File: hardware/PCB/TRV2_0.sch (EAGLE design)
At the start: 48 parts, among them IC1 TMP112, IC2 SHT21, IC4 CNY70, IC5 ATMEGA8-AU, Q1 FC-12M

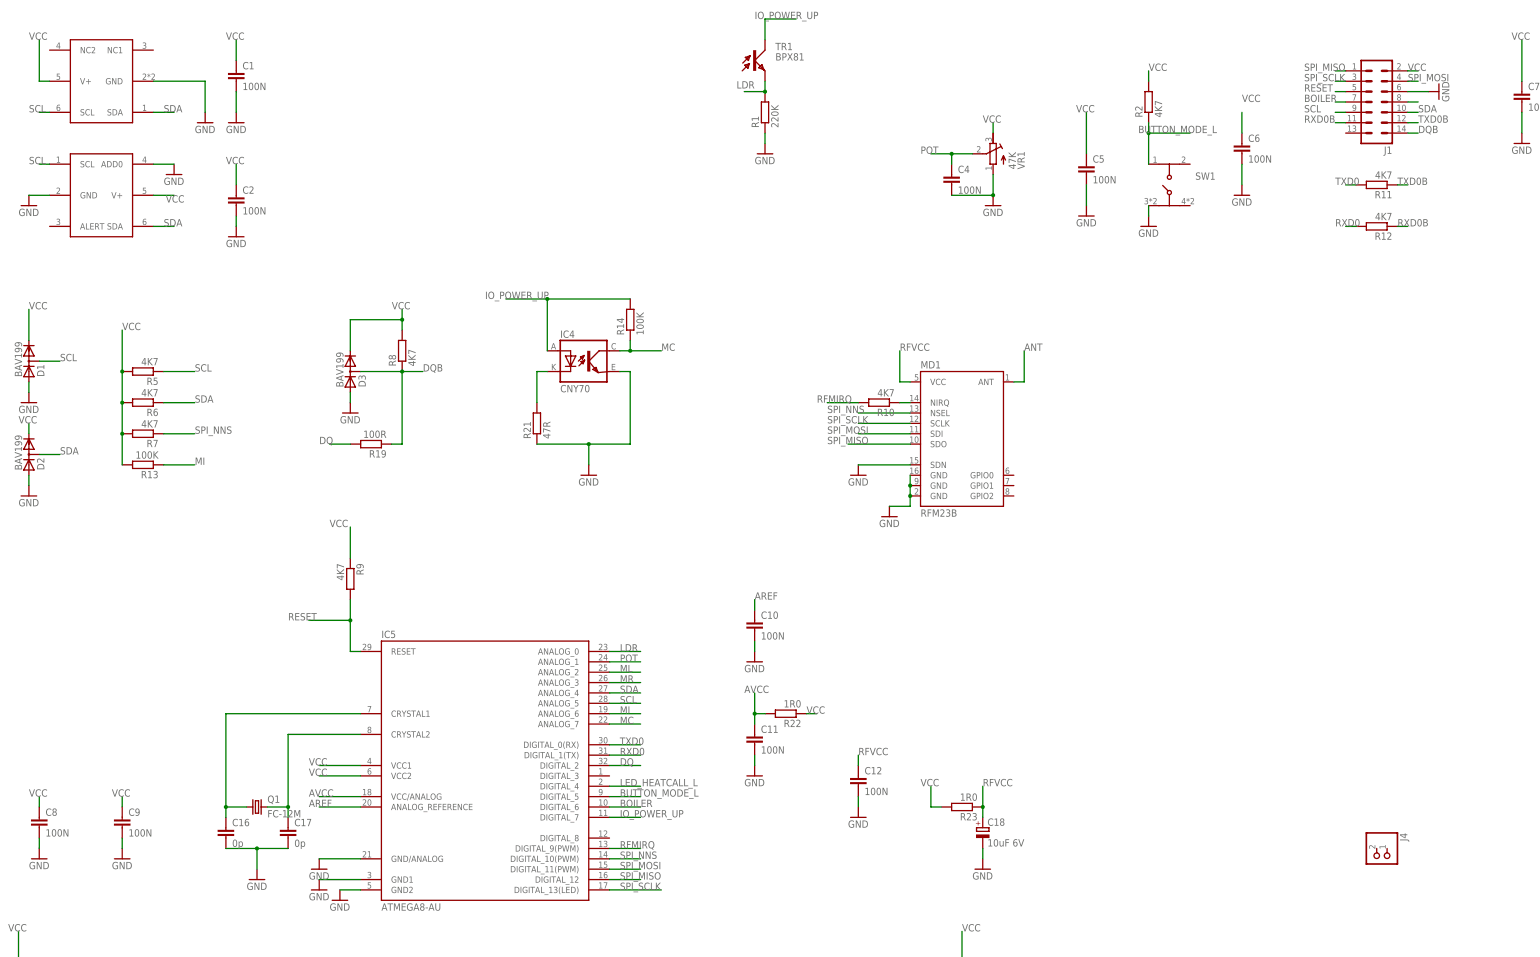
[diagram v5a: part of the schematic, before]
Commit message: removed RFM
8 pin header is just placeholder for now
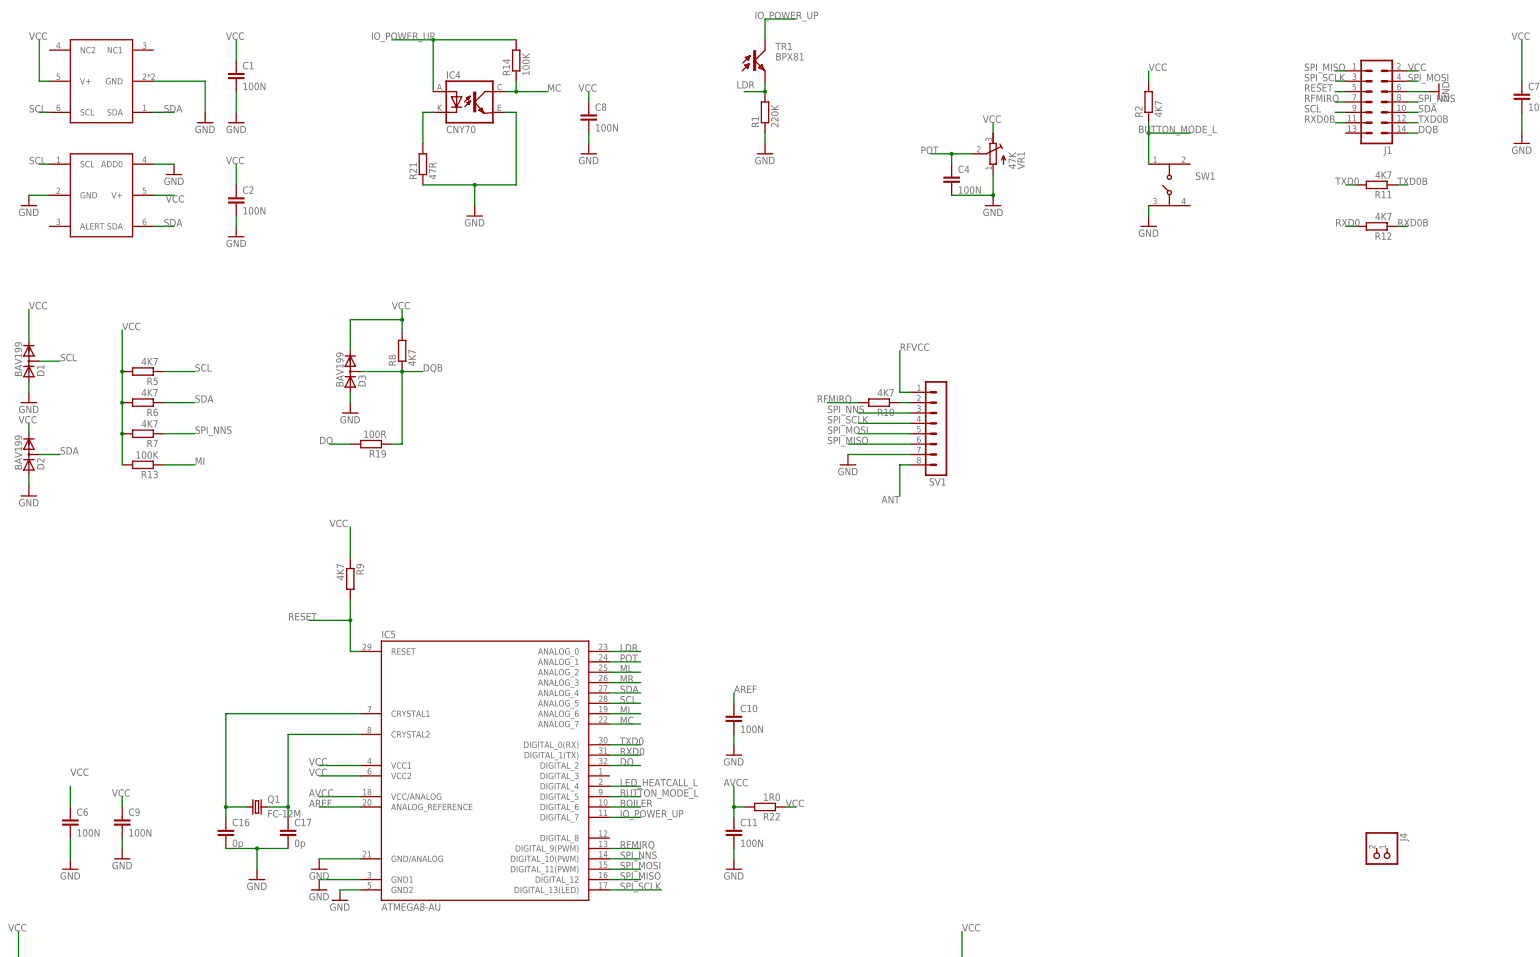
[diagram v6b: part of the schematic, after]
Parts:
- removed C12, C5: 100N, rcl:C-EUC0603
- removed C18: 10uF 6V, resistor:CPOL-EUSMCB
- removed MD1: RFM23B, SparkFun-RF:RFM23B
- removed R23: 1R0, resistor:R-EU_R0603
- added SV1: (no value), con-lstb:MA08-1
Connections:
- removed net N$2: J1.8
- net ANT: now also SV1.8; no longer MD1.ANT
- net BOILER: no longer J1.7
- net GND: now also SV1.7; no longer C12.2, C18.-, C5.2, MD1.GND@1, MD1.GND@2, MD1.GND@3, MD1.SDN
- net N$3: now also SV1.2; no longer MD1.NIRQ
- net RFMIRQ: now also J1.7
- net RFVCC: now also SV1.1; no longer C12.1, C18.+, MD1.VCC, R23.1
- net SPI_MISO: now also SV1.6; no longer MD1.SDO
- net SPI_MOSI: now also SV1.5; no longer MD1.SDI
- net SPI_NNS: now also J1.8, SV1.3; no longer MD1.NSEL
- net SPI_SCLK: now also SV1.4; no longer MD1.SCLK
- net VCC: no longer C5.1, R23.2
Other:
- moved on the sheet: C10, C11, C6, C8, IC4, R14, R21, R22

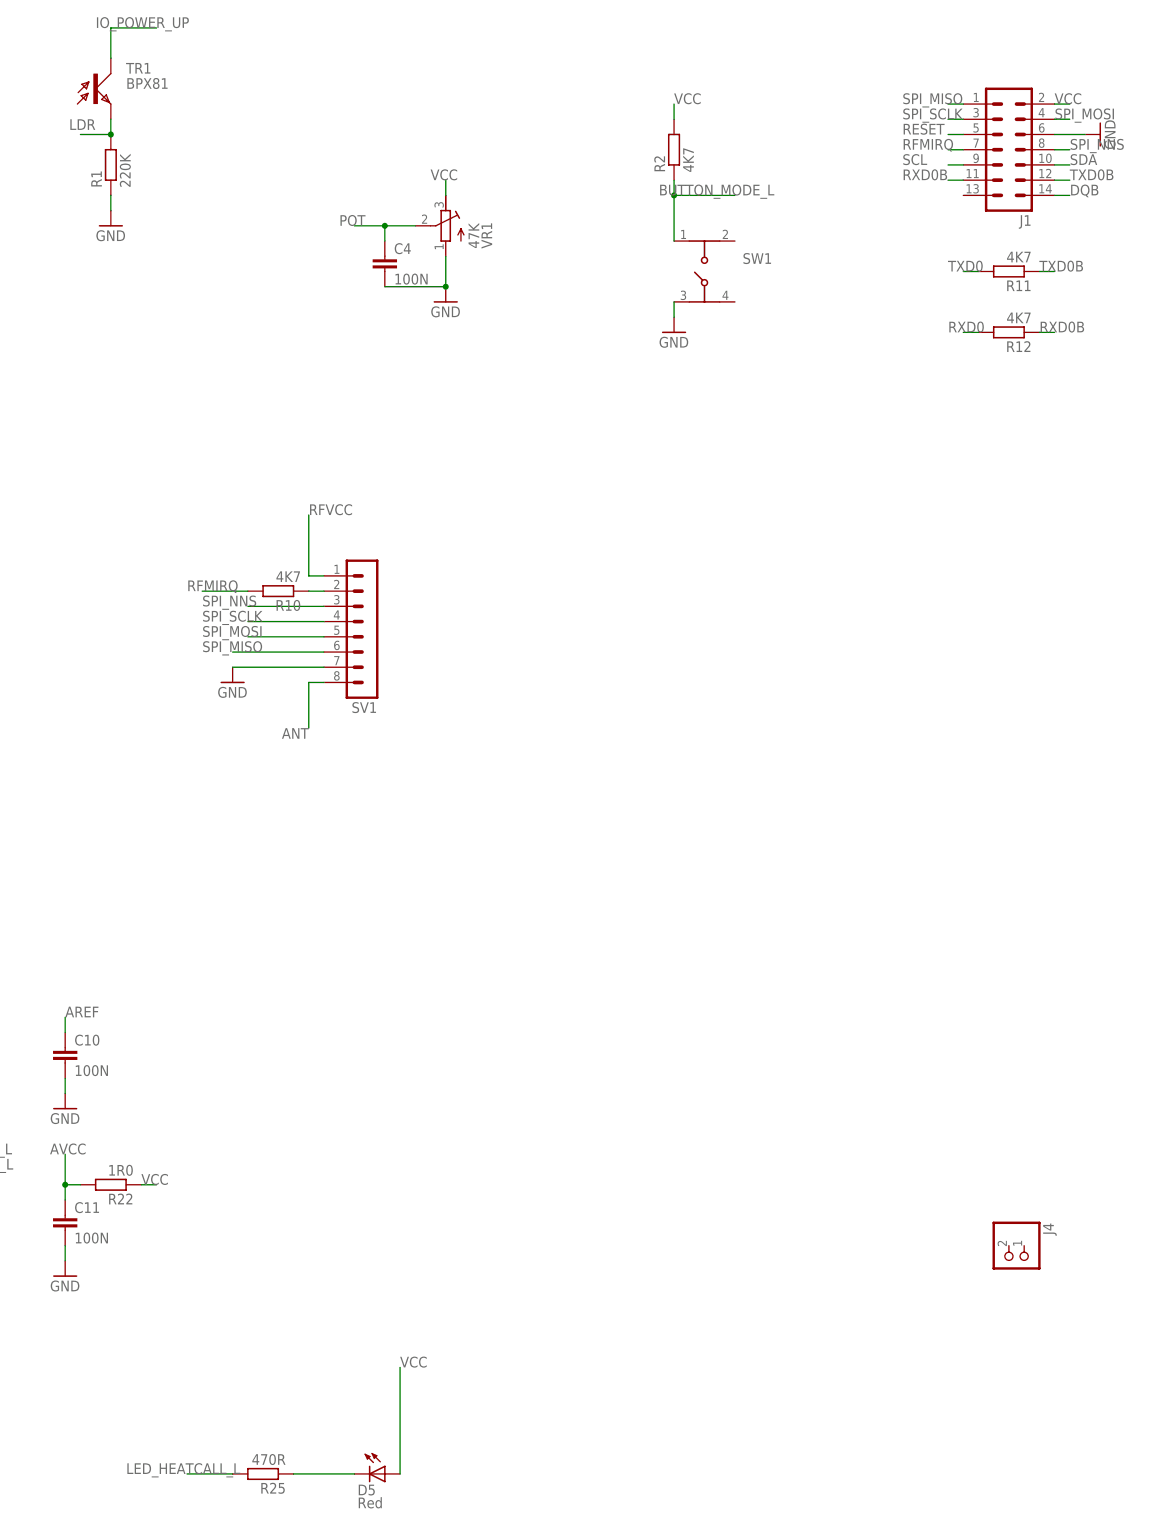
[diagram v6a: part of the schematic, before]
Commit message: SMD LED and photo added
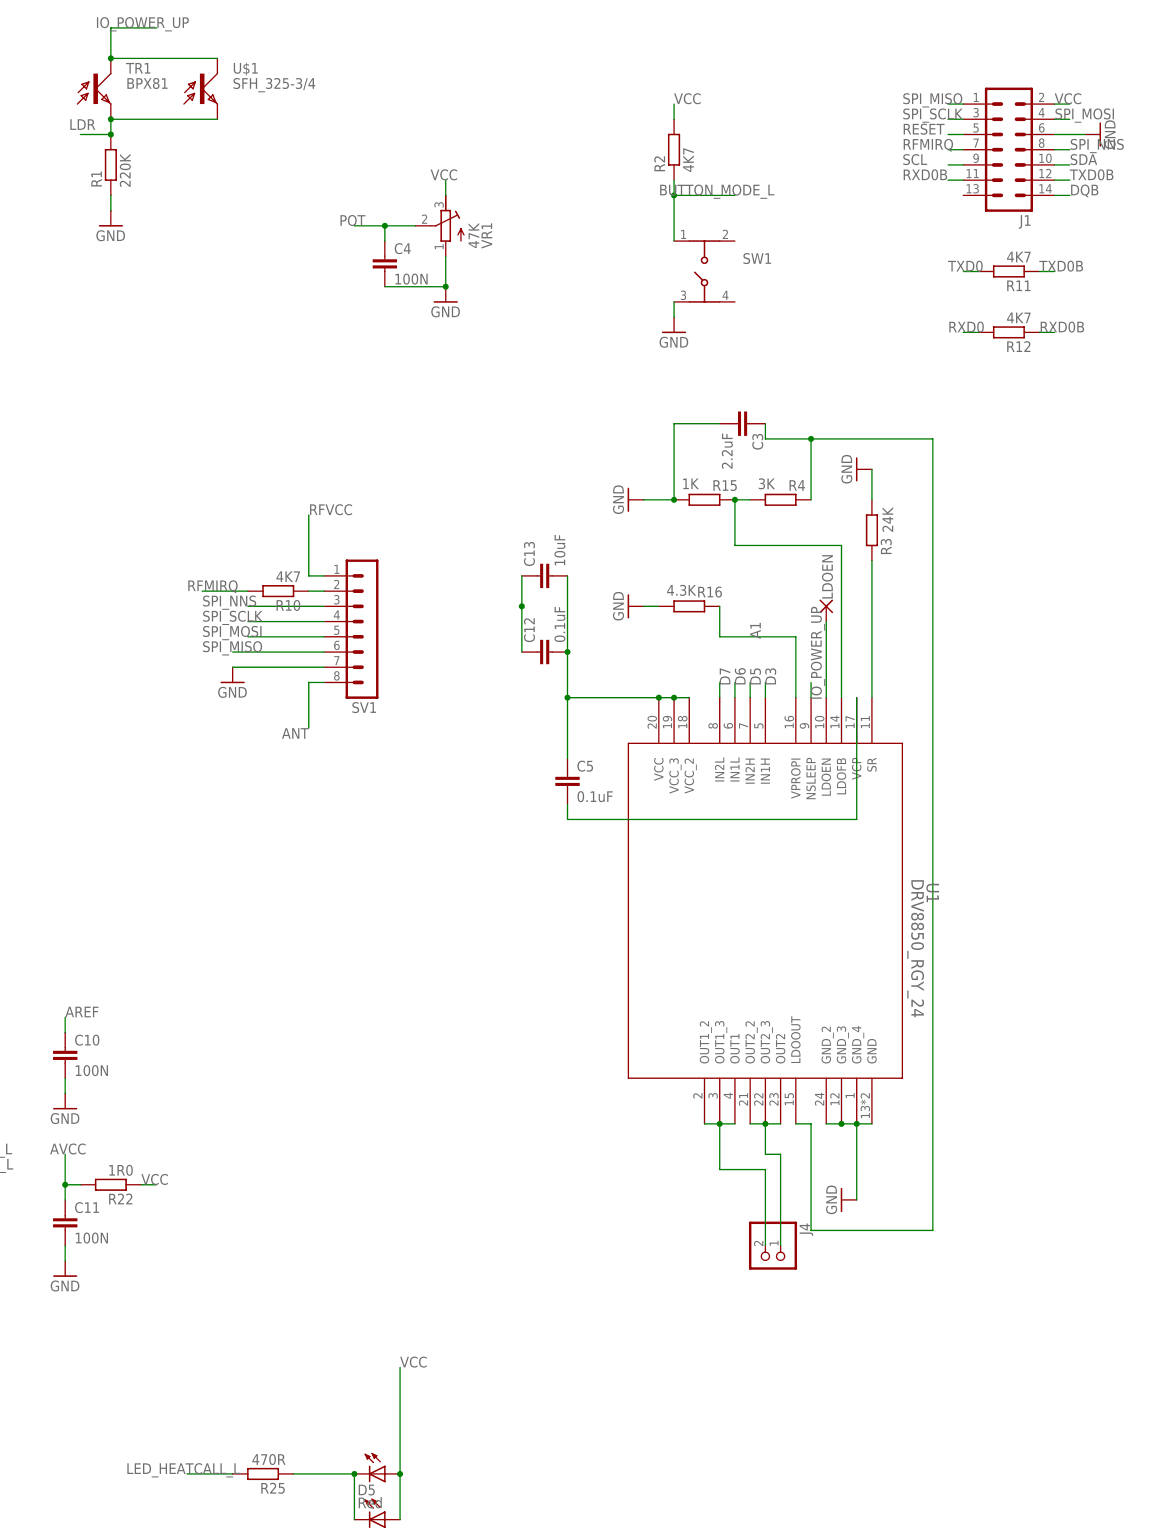
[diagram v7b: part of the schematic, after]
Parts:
- added C12, C5: 0.1uF, resistor:C-EUC0603
- added C13: 10uF, resistor:C-EUC0603
- added C3: 2.2uF, resistor:C-EUC0603
- added LDOEN: WIREPAD2,15/1,0, wirepad:WIREPAD2,15/1,0
- added R15: 1K, resistor:R-EU_R0603
- added R16: 4.3K, resistor:R-EU_R0603
- added R3: 24K, resistor:R-EU_R0603
- added R4: 3K, resistor:R-EU_R0603
- added U$1: SFH_325-3/4, opto-trans-siemens:SFH_325-3/4
- added U$2: KINGBRIGHTSIDELED, led:KINGBRIGHTSIDELED
- added U1: DRV8850_RGY_24, drv8850:DRV8850_RGY_24
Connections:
- new net A1: R16.2, U1.VPROPI
- new net D3: U1.IN1H
- new net D5: U1.IN2H
- new net D6: U1.IN1L
- new net D7: U1.IN2L
- new net N$11: J4.1, U1.OUT2, U1.OUT2_2, U1.OUT2_3
- new net N$12: R3.2, U1.SR
- new net N$14: R15.2, R4.1, U1.LDOFB
- new net N$15: C3.1, R4.2, U1.LDOOUT
- new net N$16: LDOEN.P, U1.LDOEN
- new net N$2: J4.2, U1.OUT1, U1.OUT1_2, U1.OUT1_3
- new net N$20: C5.2, U1.VCP
- new net VCC1: C12.2, C13.2, C5.1, U1.VCC, U1.VCC_2, U1.VCC_3
- net GND: now also C12.1, C13.1, C3.2, R15.1, R16.1, R3.1, U1.GND, U1.GND_2, U1.GND_3, U1.GND_4
- net IO_POWER_UP: now also U$1.C, U1.NSLEEP
- net LDR: now also U$1.E
- net N$7: now also U$2.C
- net VCC: now also U$2.A
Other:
- moved on the sheet: J4
